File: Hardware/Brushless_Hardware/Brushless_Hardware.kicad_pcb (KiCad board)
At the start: 2 copper layers, 91 parts, among them J1 RJ45_LED_Shielded, SW1 SW_Push, SW2 SW_Push, SW3 SW_Push, SW4 SW_Push, SW5 SW_Push, SW6 SW_Push, SW7 SW_DPDT_x2, U1 Teensy4.1_DEV-16771, U2 OKI, U3 TSR_1-2450

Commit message: organized components
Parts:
- moved DY10 198.6 mm to (262.3, 32.8), turned to -90 degrees
- moved Conn10 181.4 mm to (252.0, 29.6)
- moved DY8 179.0 mm to (243.2, 32.8), turned to -90 degrees
- moved DY7 171.2 mm to (233.6, 32.8), turned to -90 degrees
- moved Conn17 169.7 mm to (256.0, 66.2)
- moved Conn11 168.5 mm to (261.5, 29.6)
- moved R13 155.1 mm to (264.0, 32.8), turned to -90 degrees
- moved DY9 153.8 mm to (252.7, 32.8), turned to -90 degrees
- moved DY16 152.6 mm to (259.5, 62.1), turned to 180 degrees
- moved R12 151.9 mm to (254.5, 32.8), turned to -90 degrees
- moved R18 144.7 mm to (248.0, 60.3), turned to 180 degrees
- moved R19 144.3 mm to (259.5, 60.3), turned to 180 degrees
- moved Conn7 139.7 mm to (223.3, 29.6)
- moved Conn9 138.8 mm to (242.4, 29.6)
- moved DY3 132.8 mm to (195.7, 32.9), turned to -90 degrees
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
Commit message: more organization
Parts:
- moved C2 124.0 mm to (20.1, 53.3), turned to 180 degrees
- moved Conn19 89.8 mm to (134.0, 98.2), turned to 180 degrees
- moved SW7 79.5 mm to (160.9, 103.6), turned to -90 degrees
- moved SW1 78.0 mm to (99.7, 86.1), turned to 180 degrees
- moved R23 71.9 mm to (97.0, 82.5), turned to 180 degrees
- moved DB1 71.6 mm to (97.0, 79.4), turned to 180 degrees
- moved C3 65.6 mm to (65.9, 34.3)
- moved DG3 65.6 mm to (61.5, 29.3)
- moved R3 65.6 mm to (61.5, 31.1)
- moved U2 65.6 mm to (57.3, 33.4)
- moved C1 64.9 mm to (53.5, 35.1)
- moved C5 62.9 mm to (66.9, 24.0)
- moved DG2 62.9 mm to (61.5, 15.9)
- moved R2 62.9 mm to (61.5, 17.7)
- moved U3 62.9 mm to (57.3, 24.8)
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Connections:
- U1 pad 0: VESC_Rx_1 -> VESC_Rx_6
- U1 pad 1: VESC_Tx_1 -> VESC_Tx_6
- U1 pad 12: LIM_6 -> B4
- U1 pad 16: VESC_Rx_4 -> VESC_Rx_2
- U1 pad 17: VESC_Tx_4 -> VESC_Tx_2
- U1 pad 20: VESC_Tx_5 -> VESC_Tx_1
- U1 pad 21: VESC_Rx_5 -> VESC_Rx_1
- U1 pad 22: B1 -> LIM_1
- U1 pad 23: B2 -> LIM_2
- U1 pad 24: VESC_Tx_6 -> VESC_Tx_4
- U1 pad 25: VESC_Rx_6 -> VESC_Rx_4
- U1 pad 26: B3 -> LIM_10
- U1 pad 27: B4 -> LIM_6
- U1 pad 3: LIM_1 -> B1
- U1 pad 4: LIM_2 -> B2
- U1 pad 7: VESC_Rx_2 -> VESC_Rx_5
- U1 pad 8: VESC_Tx_2 -> VESC_Tx_5
- U1 pad 9: LIM_10 -> B3
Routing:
- added copper zone on B.Cu, net GND
- added copper zone on F.Cu, net GND

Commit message: started powerline
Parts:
- moved R6 92.3 mm to (106.6, 48.8)
- moved Conn2 92.3 mm to (85.2, 45.5)
- moved Conn3 92.3 mm to (94.6, 45.5)
- moved DY1 92.3 mm to (86.0, 48.8)
- moved DY2 92.3 mm to (95.4, 48.8)
- moved Conn4 92.3 mm to (104.0, 45.5)
- moved DY3 92.3 mm to (104.8, 48.8)
- moved R4 92.3 mm to (87.8, 48.8)
- moved R5 92.3 mm to (97.2, 48.8)
- moved Conn5 90.9 mm to (114.9, 45.5)
- moved DY4 90.9 mm to (115.7, 48.6)
- moved R7 90.9 mm to (117.5, 48.6)
- moved Conn6 89.4 mm to (125.9, 45.3)
- moved DY5 89.4 mm to (126.6, 48.5)
- moved R8 89.4 mm to (128.4, 48.5)
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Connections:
- Conn13 pad 2: ENC_1 -> ENC_2
- Conn14 pad 2: ENC_1 -> ENC_3
- Conn15 pad 2: ENC_1 -> ENC_4
- Conn16 pad 2: ENC_1 -> ENC_5
- Conn17 pad 2: ENC_1 -> ENC_6
- DB1 pad 2: +3V3 -> +3.3V
- DB2 pad 2: +3V3 -> +3.3V
- DB3 pad 2: +3V3 -> +3.3V
- DB4 pad 2: +3V3 -> +3.3V
- DB5 pad 2: +3V3 -> +3.3V
- DB6 pad 2: +3V3 -> +3.3V
- DY12 pad 2: ENC_1 -> ENC_2
- DY13 pad 2: ENC_1 -> ENC_3
- DY14 pad 2: ENC_1 -> ENC_4
- DY15 pad 2: ENC_1 -> ENC_5
- DY16 pad 2: ENC_1 -> ENC_6
- R20 pad 1: +3V3 -> +3.3V
- R21 pad 1: +3V3 -> +3.3V
- R22 pad 1: +3V3 -> +3.3V
- R26 pad 1: +3V3 -> +3.3V
- R27 pad 1: +3V3 -> +3.3V
- R28 pad 1: +3V3 -> +3.3V
- U1 pad 10: LIM_9 -> LIM_4
- U1 pad 11: LIM_7 -> ENC_6
- U1 pad 13: LIM_4 -> LIM_9
- U1 pad 18: LIM_5 -> LIM_7
- U1 pad 19: LIM_8 -> LIM_5
- U1 pad 22: LIM_1 -> LIM_3
- U1 pad 23: LIM_2 -> LIM_1
- U1 pad 26: LIM_10 -> ENC_1
- U1 pad 27: LIM_6 -> ENC_5
- U1 pad 33: LIM_3 -> LIM_10
- U1 pad 34: ENC_6 -> LIM_8
- U1 pad 35: ENC_5 -> LIM_6
- U1 pad 41: ENC_1 -> LIM_2
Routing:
- net +3.3V: track 0.00 -> 253.9 mm, vias 0 -> 1
- net +5V: track 0.00 -> 222.3 mm, vias 0 -> 1
- net +36V: track 0.00 -> 52.3 mm
- net VESC_Rx_3: track 0.00 -> 36.3 mm, vias 0 -> 2
- net VESC_Rx_1: track 0.00 -> 36.1 mm
- net VESC_Tx_1: track 0.00 -> 31.0 mm
- net VESC_Rx_2: track 0.00 -> 28.9 mm
- net VESC_Tx_3: track 0.00 -> 28.2 mm
- net VESC_Tx_2: track 0.00 -> 28.2 mm
- net ENC_4: track 0.00 -> 4.21 mm
- net ENC_2: track 0.00 -> 4.21 mm
- net ENC_6: track 0.00 -> 4.08 mm
- net ENC_5: track 0.00 -> 4.08 mm
- net ENC_3: track 0.00 -> 4.08 mm
- net ENC_1: track 0.00 -> 4.07 mm
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
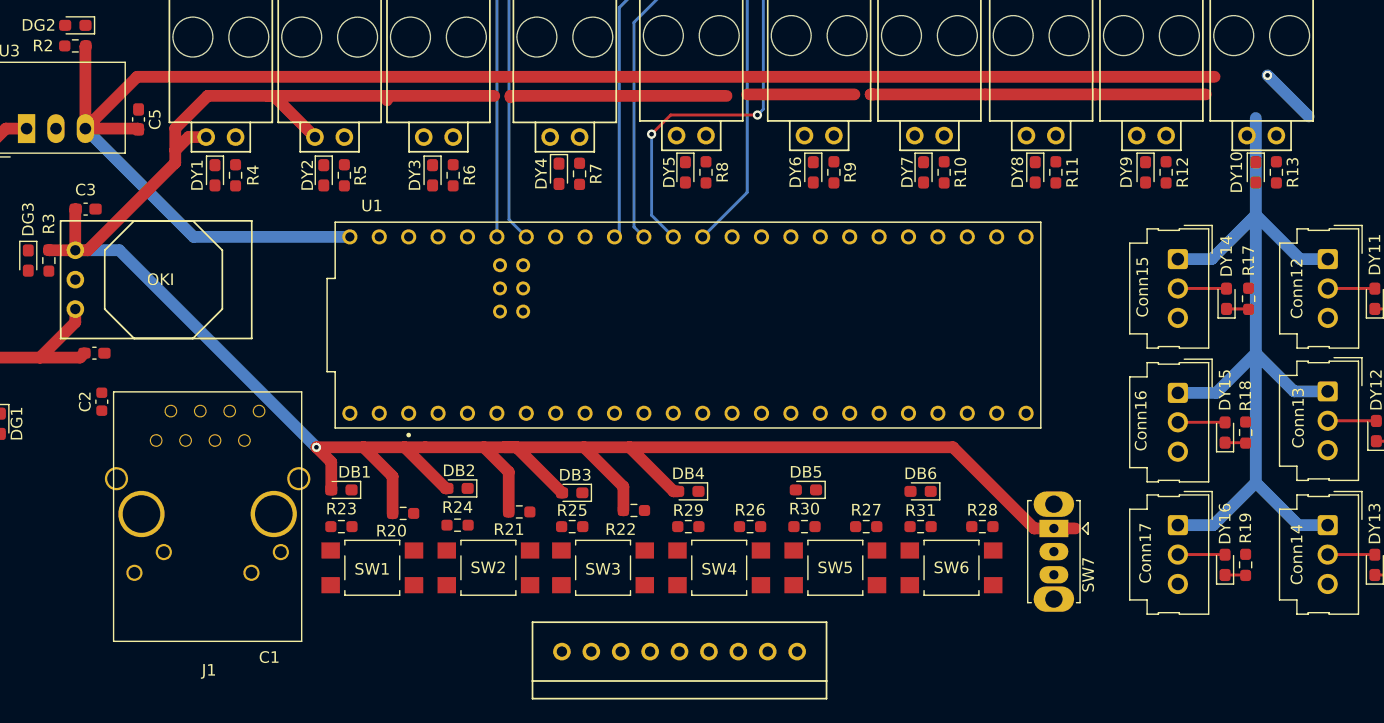
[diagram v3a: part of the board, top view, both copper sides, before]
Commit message: started doing traces
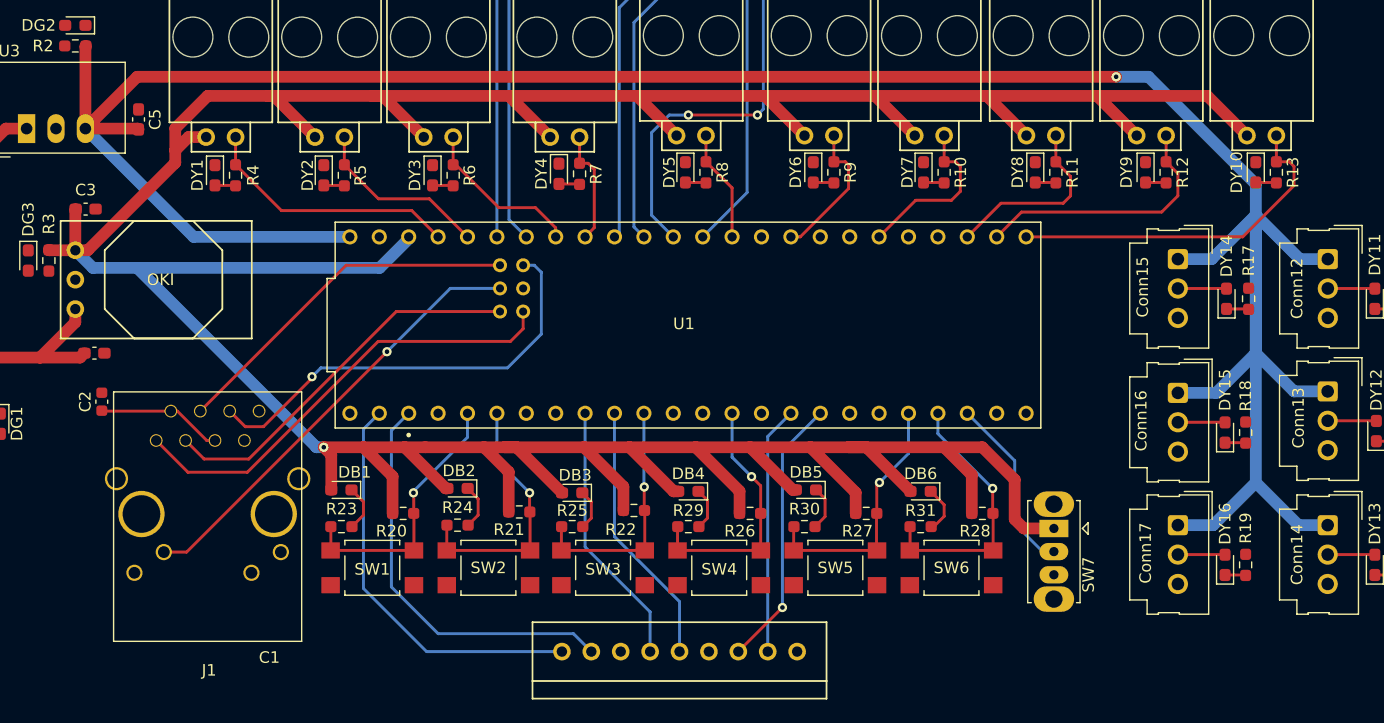
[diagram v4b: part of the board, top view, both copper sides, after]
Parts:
- moved R26 1.14 mm to (132.2, 78.0)
- moved R27 1.14 mm to (142.2, 78.0)
- moved R28 1.14 mm to (152.3, 78.0)
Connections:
- U1 pad 10: LIM_4 -> ENC_4
- U1 pad 3.3V_1: +3V3 -> +3.3V
- U1 pad 3.3V_2: +3V3 -> +3.3V
- U1 pad 38: ENC_4 -> LIM_4
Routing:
- net +3.3V: track 253.9 -> 356.9 mm
- net Tx+: track 0.00 -> 39.5 mm
- net LED: track 0.00 -> 38.5 mm, vias 0 -> 1
- net Rx-: track 0.00 -> 38.0 mm, vias 0 -> 1
- net VESC_Tx_6: track 0.00 -> 35.2 mm
- net VESC_Rx_6: track 0.00 -> 35.1 mm
- net Tx-: track 0.00 -> 33.1 mm
- net Rx+: track 0.00 -> 31.1 mm
- net LIM_10: track 0.00 -> 30.6 mm
- net VESC_Rx_4: track 0.00 -> 23.5 mm, vias 0 -> 1
- net B6: track 0.00 -> 23.1 mm, vias 0 -> 1
- net B1: track 0.00 -> 23.1 mm, vias 0 -> 1
- net VESC_Tx_5: track 0.00 -> 22.9 mm
- net VESC_Rx_5: track 0.00 -> 22.9 mm
- net LIM_8: track 0.00 -> 22.7 mm
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
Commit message: finished pcb
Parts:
- added V1: Via, MRDT_Drill_Holes:4_40_Hole_Corner, F.Cu at (54.0, 24.3)
- added V2: Via, MRDT_Drill_Holes:4_40_Hole_Corner, F.Cu at (188.7, 94.1)
- added V3: Via, MRDT_Drill_Holes:4_40_Hole_Corner, F.Cu at (188.7, 24.3)
- added V4: Via, MRDT_Drill_Holes:4_40_Hole_Corner, F.Cu at (54.0, 94.1)
- moved R16 31.0 mm to (160.9, 67.2)
- moved DY13 31.0 mm to (159.2, 67.2)
- moved DY16 27.7 mm to (159.3, 58.6)
- moved R19 27.7 mm to (161.0, 58.6)
- moved DY14 21.2 mm to (158.9, 74.9)
- moved R17 21.2 mm to (160.8, 74.9)
- moved Conn17 21.0 mm to (170.1, 58.0), turned to 180 degrees
- moved Conn15 17.9 mm to (170.1, 73.9), turned to 180 degrees
- moved Conn14 17.8 mm to (170.1, 65.9), turned to 180 degrees
- moved Conn12 17.3 mm to (176.5, 72.4), turned to 0 degrees
- moved DY15 17.0 mm to (185.5, 59.2)
- moved R18 17.0 mm to (187.3, 59.2)
- moved DY11 15.8 mm to (185.8, 75.2)
- moved R14 15.8 mm to (187.7, 75.2)
- moved Conn1 14.6 mm to (72.2, 69.4)
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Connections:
- U1 pad 10: ENC_4 -> unconnected-(U1-Pad10)
- U1 pad 11: ENC_6 -> unconnected-(U1-Pad11)
- U1 pad 26: ENC_1 -> ENC_2
- U1 pad 27: ENC_5 -> ENC_3
- U1 pad 31: unconnected-(U1-Pad31) -> ENC_4
- U1 pad 32: unconnected-(U1-Pad32) -> ENC_1
- U1 pad 33: LIM_10 -> ENC_5
- U1 pad 34: LIM_8 -> ENC_6
- U1 pad 35: LIM_6 -> LIM_10
- U1 pad 36: unconnected-(U1-Pad36) -> LIM_8
- U1 pad 37: unconnected-(U1-Pad37) -> LIM_6
- U1 pad 39: ENC_3 -> unconnected-(U1-Pad39)
- U1 pad 40: ENC_2 -> unconnected-(U1-Pad40)
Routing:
- net ENC_2: track 4.21 -> 50.3 mm
- net +5V: track 230.9 -> 190.6 mm
- net ENC_1: track 4.07 -> 32.0 mm
- net ENC_5: track 4.08 -> 32.0 mm
- net ENC_3: track 4.08 -> 26.6 mm
- net +36V: track 52.3 -> 74.1 mm
- net ENC_4: track 4.21 -> 17.2 mm
- net ENC_6: track 4.08 -> 16.5 mm
- net Rx+: track 31.1 -> 39.4 mm
- net Tx-: track 33.1 -> 39.7 mm
- net +3.3V: track 356.9 -> 362.5 mm
- net LIM_10: track 30.6 -> 36.0 mm
- net LIM_8: track 22.7 -> 28.1 mm
- net LIM_6: track 16.1 -> 21.1 mm
- net SW: track 15.6 -> 17.8 mm
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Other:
- board outline added: 134.7 x 69.8 mm

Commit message: worked on fixing the board for a bit
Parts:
- added Conn20: Molex_SL_03, MRDT_Connectors:MOLEX_SL_03_Vertical, F.Cu at (127.4, 108.6)
- added Conn21: Molex_SL_03, MRDT_Connectors:MOLEX_SL_03_Vertical, F.Cu at (127.4, 100.8)
- added Conn22: Molex_SL_03, MRDT_Connectors:MOLEX_SL_03_Vertical, F.Cu at (116.1, 100.8)
- added Conn23: Molex_SL_03, MRDT_Connectors:MOLEX_SL_03_Vertical, F.Cu at (116.1, 108.6)
- Conn18, Conn19: value Molex_SL_09 -> Molex_SL_03; footprint MRDT_Connectors:MOLEX_SL_09_Vertical -> MRDT_Connectors:MOLEX_SL_03_Vertical
- R10, R11, R12, R13, R4, R5, R6, R7, R8, R9: value 43 -> 100
- moved Conn18 81.1 mm to (143.1, 105.0), turned to 180 degrees
- moved Conn19 25.8 mm to (155.4, 107.2)
- moved R14 14.3 mm to (174.0, 71.1), turned to -90 degrees
- moved R15 14.1 mm to (174.1, 63.2), turned to -90 degrees
- moved R18 13.7 mm to (174.2, 55.1), turned to -90 degrees
- moved DY12 10.7 mm to (175.9, 63.2), turned to -90 degrees
- moved DY11 10.7 mm to (175.9, 71.1), turned to -90 degrees
- moved DY15 10.4 mm to (176.0, 55.1), turned to -90 degrees
- moved Conn12 8.77 mm to (185.2, 73.9), turned to 180 degrees
- moved Conn13 8.75 mm to (185.2, 66.0), turned to 180 degrees
- moved Conn16 8.36 mm to (184.9, 57.8), turned to 180 degrees
- moved C2 4.95 mm to (76.1, 73.3)
- moved J1 4.95 mm to (85.6, 96.0)
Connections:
- Conn19 pad 2: VESC_Tx_4 -> VESC_Tx_2
- Conn19 pad 3: VESC_Rx_4 -> VESC_Rx_2
- U1 pad R-: (no net) -> Rx-
- U1 pad T-: (no net) -> Tx-
- U1 pad VIN: +5V -> unconnected-(U1-PadVIN)
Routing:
- net LED: track 38.5 -> 0.00 mm, vias 1 -> 0
- net VESC_Rx_3: track 36.4 -> 0.00 mm, vias 2 -> 0
- net VESC_Rx_1: track 36.1 -> 0.00 mm
- net +5V: track 190.6 -> 222.9 mm
- net VESC_Tx_1: track 31.0 -> 0.00 mm
- net VESC_Rx_2: track 28.9 -> 0.00 mm
- net VESC_Tx_3: track 28.2 -> 0.00 mm
- net VESC_Tx_2: track 28.2 -> 0.00 mm
- net Rx+: track 39.4 -> 33.2 mm, vias 0 -> 1
- net Rx-: track 38.0 -> 33.5 mm, vias 1 -> 2
- net Tx+: track 39.8 -> 44.3 mm
- net Tx-: track 39.7 -> 44.2 mm
- net ENC_5: track 32.0 -> 29.6 mm
- net ENC_1: track 32.0 -> 29.8 mm
- net Net-(DG3-Pad2): track 0.00 -> 1.79 mm
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
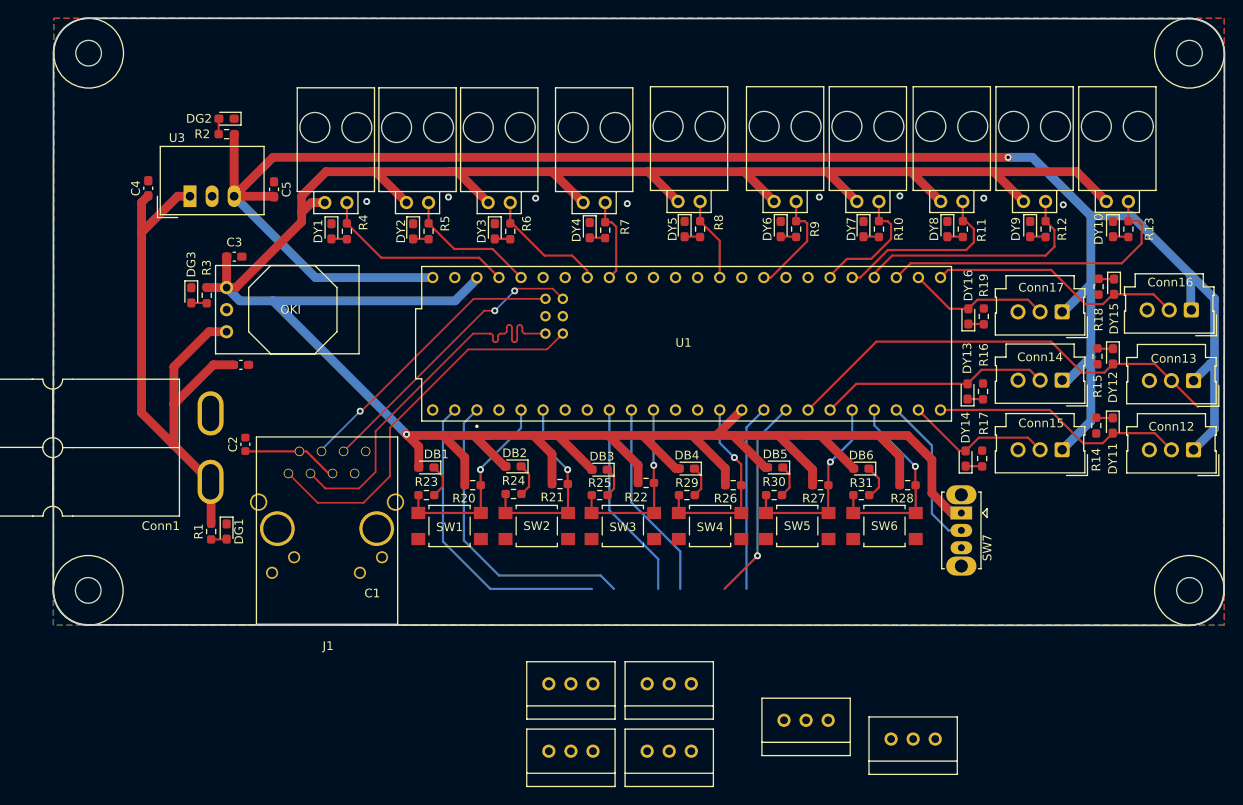
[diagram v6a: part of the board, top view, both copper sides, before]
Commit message: fixed placement and redid board
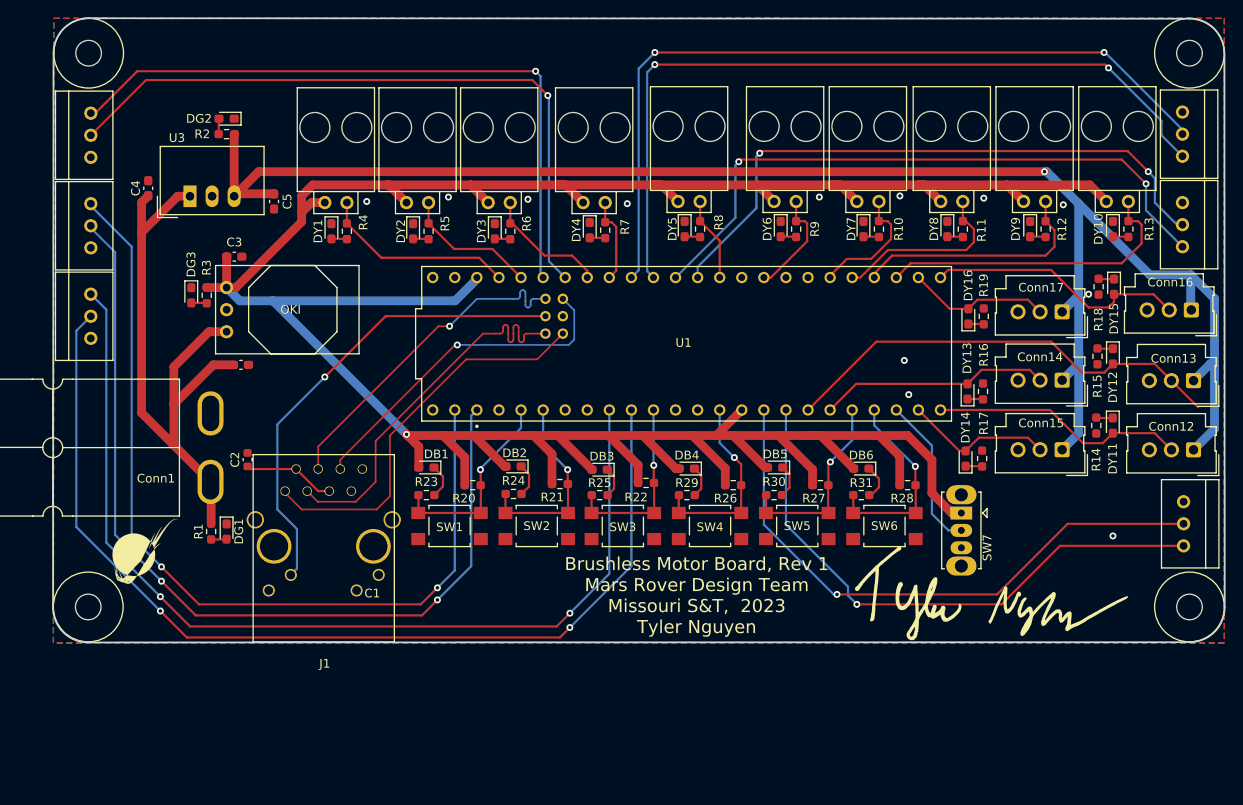
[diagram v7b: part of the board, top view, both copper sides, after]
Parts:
- added G***: LOGO, Gimbal_Board_Library:z-sig-Tyler-Nguyen, F.Cu at (161.2, 90.5)
- added G***: LOGO, MRDT_Silkscreens:0_MRDT_Logo_7.5mm, F.Cu at (64.5, 85.6)
- moved Conn20 97.2 mm to (58.3, 40.3), turned to 90 degrees
- moved Conn21 85.4 mm to (58.3, 50.7), turned to 90 degrees
- moved Conn18 81.0 mm to (183.9, 35.1), turned to -90 degrees
- moved Conn23 74.8 mm to (58.3, 61.1), turned to 90 degrees
- moved Conn22 71.1 mm to (184.0, 79.9), turned to -90 degrees
- moved Conn19 68.0 mm to (183.9, 45.5), turned to -90 degrees
- moved J1 2.07 mm to (85.2, 98.0)
- moved V2 1.91 mm to (188.7, 96.0)
- moved V4 1.91 mm to (54.0, 96.0)
- moved C2 1.78 mm to (76.3, 75.0)
- moved C5 1.40 mm to (79.4, 45.3), turned to 90 degrees
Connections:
- U1 pad 0: VESC_Rx_6 -> VESC_Rx_4
- U1 pad 1: VESC_Tx_6 -> VESC_Tx_4
- U1 pad 14: VESC_Tx_3 -> VESC_Tx_2
- U1 pad 15: VESC_Rx_3 -> VESC_Rx_2
- U1 pad 16: VESC_Rx_2 -> VESC_Rx_1
- U1 pad 17: VESC_Tx_2 -> VESC_Tx_1
- U1 pad 20: VESC_Tx_1 -> VESC_Tx_3
- U1 pad 21: VESC_Rx_1 -> VESC_Rx_3
- U1 pad 24: VESC_Tx_4 -> VESC_Tx_5
- U1 pad 25: VESC_Rx_4 -> VESC_Rx_5
- U1 pad 7: VESC_Rx_5 -> VESC_Rx_6
- U1 pad 8: VESC_Tx_5 -> VESC_Tx_6
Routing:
- net VESC_Tx_1: track 0.00 -> 91.9 mm, vias 0 -> 2
- net VESC_Rx_1: track 0.00 -> 91.2 mm, vias 0 -> 2
- net VESC_Tx_4: track 21.4 -> 102.1 mm, vias 0 -> 2
- net VESC_Tx_6: track 35.2 -> 115.4 mm, vias 0 -> 2
- net VESC_Tx_3: track 0.00 -> 78.1 mm, vias 0 -> 1
- net VESC_Rx_3: track 0.00 -> 77.7 mm, vias 0 -> 1
- net VESC_Rx_6: track 35.1 -> 112.7 mm, vias 0 -> 2
- net VESC_Rx_4: track 23.5 -> 100.8 mm, vias 1 -> 2
- net VESC_Rx_2: track 0.00 -> 73.4 mm, vias 0 -> 2
- net VESC_Tx_2: track 0.00 -> 71.3 mm, vias 0 -> 2
- net LED: track 0.00 -> 54.5 mm, vias 0 -> 1
- net VESC_Tx_5: track 22.9 -> 68.2 mm, vias 0 -> 1
- net VESC_Rx_5: track 22.9 -> 66.1 mm, vias 0 -> 1
- net +5V: track 222.9 -> 193.6 mm
- net +3.3V: track 362.5 -> 345.4 mm
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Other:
- board size 134.7 x 69.8 mm -> 134.8 x 71.8 mm
- board text added: "Brushless Motor Board, Rev 1 Mars Rover Design Team Missouri S&T, 2023 Tyler Nguyen"
